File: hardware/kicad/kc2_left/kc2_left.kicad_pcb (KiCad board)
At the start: 2 copper layers, 147.2 x 133.8 mm, 70 parts, among them SW1 KEY_01, SW10 KEY_10, SW11 KEY_11, SW12 KEY_12, SW13 KEY_13, SW14 KEY_14, SW15 KEY_15, SW16 KEY_16, SW17 KEY_17, SW18 KEY_18, SW19 KEY_19, SW2 KEY_02, SW20 KEY_20, SW21 KEY_21, SW22 KEY_22, SW23 KEY_23, SW24 KEY_24, SW25 KEY_25, SW26 KEY_26, SW27 KEY_27, SW28 KEY_28, SW29 KEY_29, SW3 KEY_03, SW30 KEY_30, SW31 KEY_31, SW32 KEY_32, SW4 KEY_04, SW5 KEY_05, SW6 KEY_06, SW7 KEY_07, SW8 KEY_08, SW9 KEY_09, U1 nice!nano_v2_socket_24pin

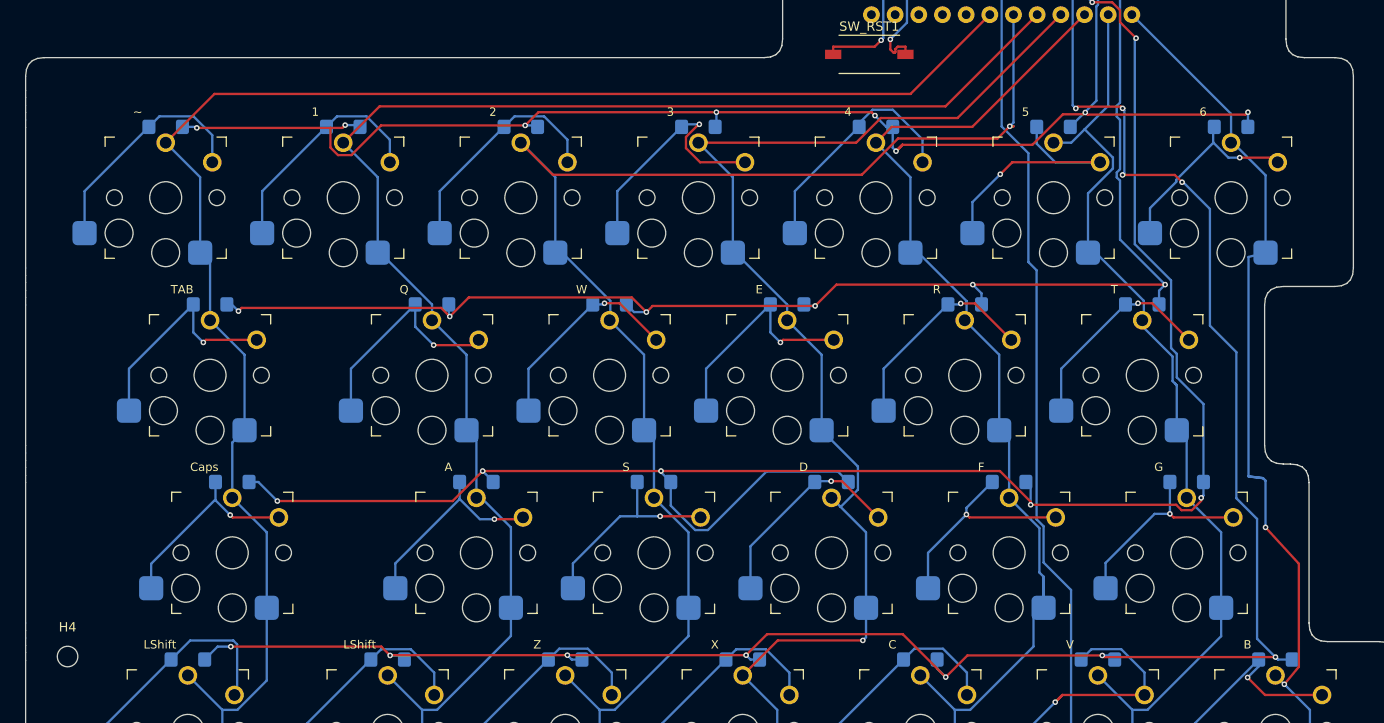
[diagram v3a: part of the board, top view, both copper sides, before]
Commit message: fix: KC2 X3 H4/H5 마운팅 홀 배치 조정
H4를 한 줄 위로 옮기고 H2 인접 상단 코너에 H5를 추가해 하부 바닥판 고정 지점 분포를 개선
왼쪽은 상단 외곽 제약 때문에 H2.x보다 안쪽인 x=173.45에 H5를 배치
관련 산출물과 검증 증거를 동일 보드 상태로 재생성
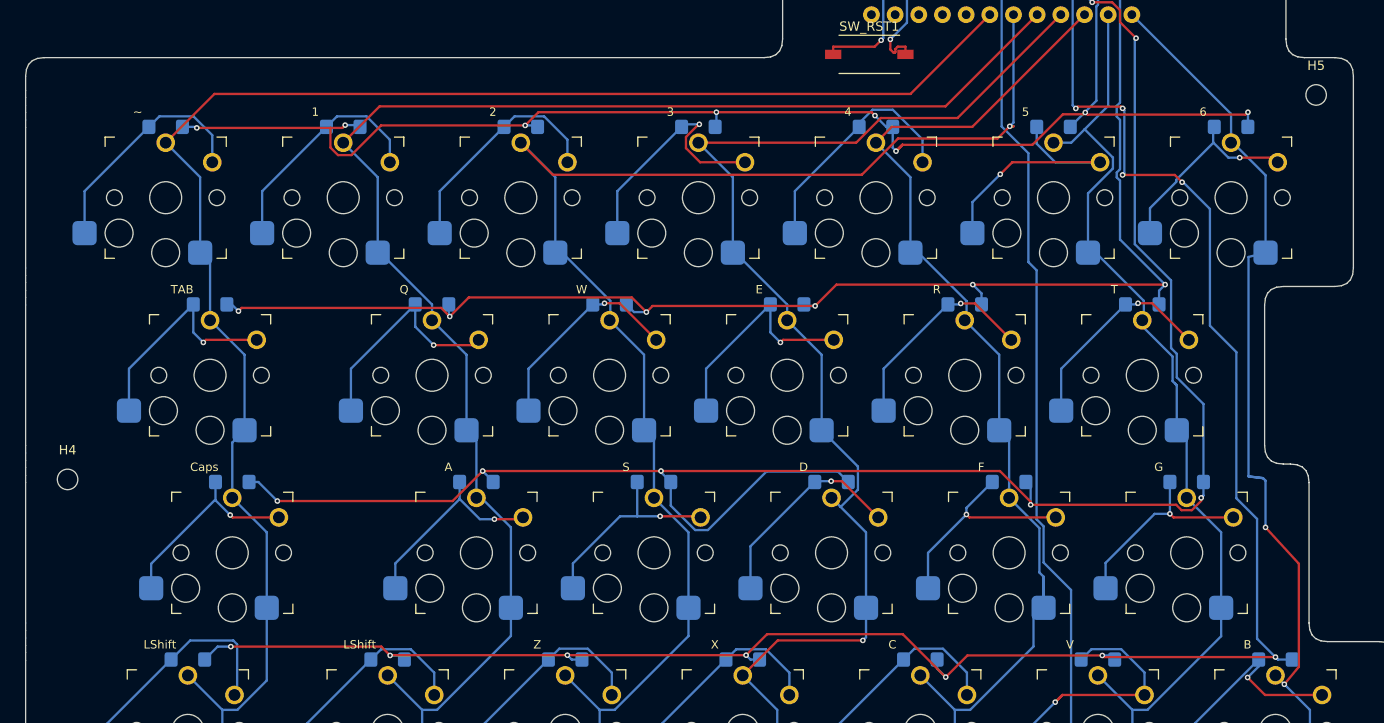
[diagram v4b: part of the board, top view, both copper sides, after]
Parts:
- added H5: M2_NPTH_2.2, MountingHole_2.2mm_M2, F.Cu at (173.4, 66.5)
- moved H4 19.0 mm to (39.5, 107.8)
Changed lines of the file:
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@@
 	(footprint "MountingHole_2.2mm_M2"
 		(layer "F.Cu")
-		(at 39.5 126.75)
+		(at 39.5 107.75)
 		(descr "Mounting Hole 2.2mm, M2, no annular, generated by kicad-footprint-generator mountinghole.py")
 		(tags "mountinghole M2")
@@
 		(embedded_fonts no)
 	)
+	(footprint "MountingHole_2.2mm_M2"
+		(layer "F.Cu")
+		(at 173.45 66.5)
+		(descr "Mounting Hole 2.2mm, M2, no annular, generated by kicad-footprint-generator mountinghole.py")
+		(tags "mountinghole M2")
+		(property "Reference" "H5"
+			(at 0 -3.15 0)
+			(layer "F.SilkS")
+			(effects
+				(font
+					(size 1 1)
+					(thickness 0.15)
+				)
+			)
+		)
+		(property "Value" "M2_NPTH_2.2"
+			(at 0 3.15 0)
+			(layer "F.Fab")
+			(effects
+				(font
+					(size 1 1)
+					(thickness 0.15)
+				)
+			)
+		)
+		(property "Datasheet" ""
+			(at 0 0 0)
+			(layer "F.Fab")
+			(hide yes)
+			(effects
+				(font
+					(size 1.27 1.27)
+				)
+			)
+		)
+		(property "Description" ""
+			(at 0 0 0)
+			(layer "F.Fab")
+			(hide yes)
+			(effects
+				(font
+					(size 1.27 1.27)
+				)
+			)
+		)
+		(property "KiLib_Generator" "mounting_hardware/mounting_hole"
+			(at 0 0 0)
+			(layer "F.SilkS")
+			(hide yes)
+			(effects
+				(font
+					(size 1 1)
+					(thickness 0.15)
+				)
+			)
+		)
+		(attr exclude_from_pos_files exclude_from_bom)
+		(duplicate_pad_numbers_are_jumpers no)
+		(fp_circle
+			(center 0 0)
+			(end 2.2 0)
+			(stroke
+				(width 0.15)
+				(type solid)
+			)
+			(fill no)
+			(layer "Cmts.User")
+		)
+		(fp_circle
+			(center 0 0)
+			(end 2.45 0)
+			(stroke
+				(width 0.05)
+				(type solid)
+			)
+			(fill no)
+			(layer "F.CrtYd")
+		)
+		(fp_text user "${REFERENCE}"
+			(at 0 0 0)
+			(layer "F.Fab")
+			(effects
+				(font
+					(size 1 1)
+					(thickness 0.15)
+				)
+			)
+		)
+		(pad "" np_thru_hole circle
+			(at 0 0)
+			(size 2.2 2.2)
+			(drill 2.2)
+			(layers "*.Cu" "*.Mask")
+		)
+		(embedded_fonts no)
+	)
 	(footprint "SW_Kailh_Choc_V1_HotSwap_THT"
 		(layer "F.Cu")
@@
 	)
 	(gr_line
-		(start 37 124.25)
-		(end 42 124.25)
+		(start 37 105.25)
+		(end 42 105.25)
 		(stroke
 			(width 0.08)
@@
 	)
 	(gr_line
-		(start 37 129.25)
-		(end 37 124.25)
+		(start 37 110.25)
+		(end 37 105.25)
 		(stroke
 			(width 0.08)
@@
 	)
 	(gr_line
-		(start 42 124.25)
-		(end 42 129.25)
+		(start 42 105.25)
+		(end 42 110.25)
 		(stroke
 			(width 0.08)
@@
 	)
 	(gr_line
-		(start 42 129.25)
-		(end 37 129.25)
+		(start 42 110.25)
+		(end 37 110.25)
 		(stroke
 			(width 0.08)
@@
 	)
 	(gr_line
+		(start 170.95 64)
+		(end 175.95 64)
+		(stroke
+			(width 0.08)
+			(type default)
+		)
+		(layer "Cmts.User")
+	)
+	(gr_line
+		(start 170.95 69)
+		(end 170.95 64)
+		(stroke
+			(width 0.08)
+			(type default)
+		)
+		(layer "Cmts.User")
+	)
+	(gr_line
 		(start 175.7125 162.25)
 		(end 180.7125 162.25)
@@
 		(stroke
 			(width 0.08)
+			(type default)
+		)
+		(layer "Cmts.User")
+	)
+	(gr_line
+		(start 175.95 64)
+		(end 175.95 69)
+		(stroke
+			(width 0.08)
+			(type default)
+		)
+		(layer "Cmts.User")
+	)
+	(gr_line
+		(start 175.95 69)
+		(end 170.95 69)
+		(stroke
+			(width 0.08)

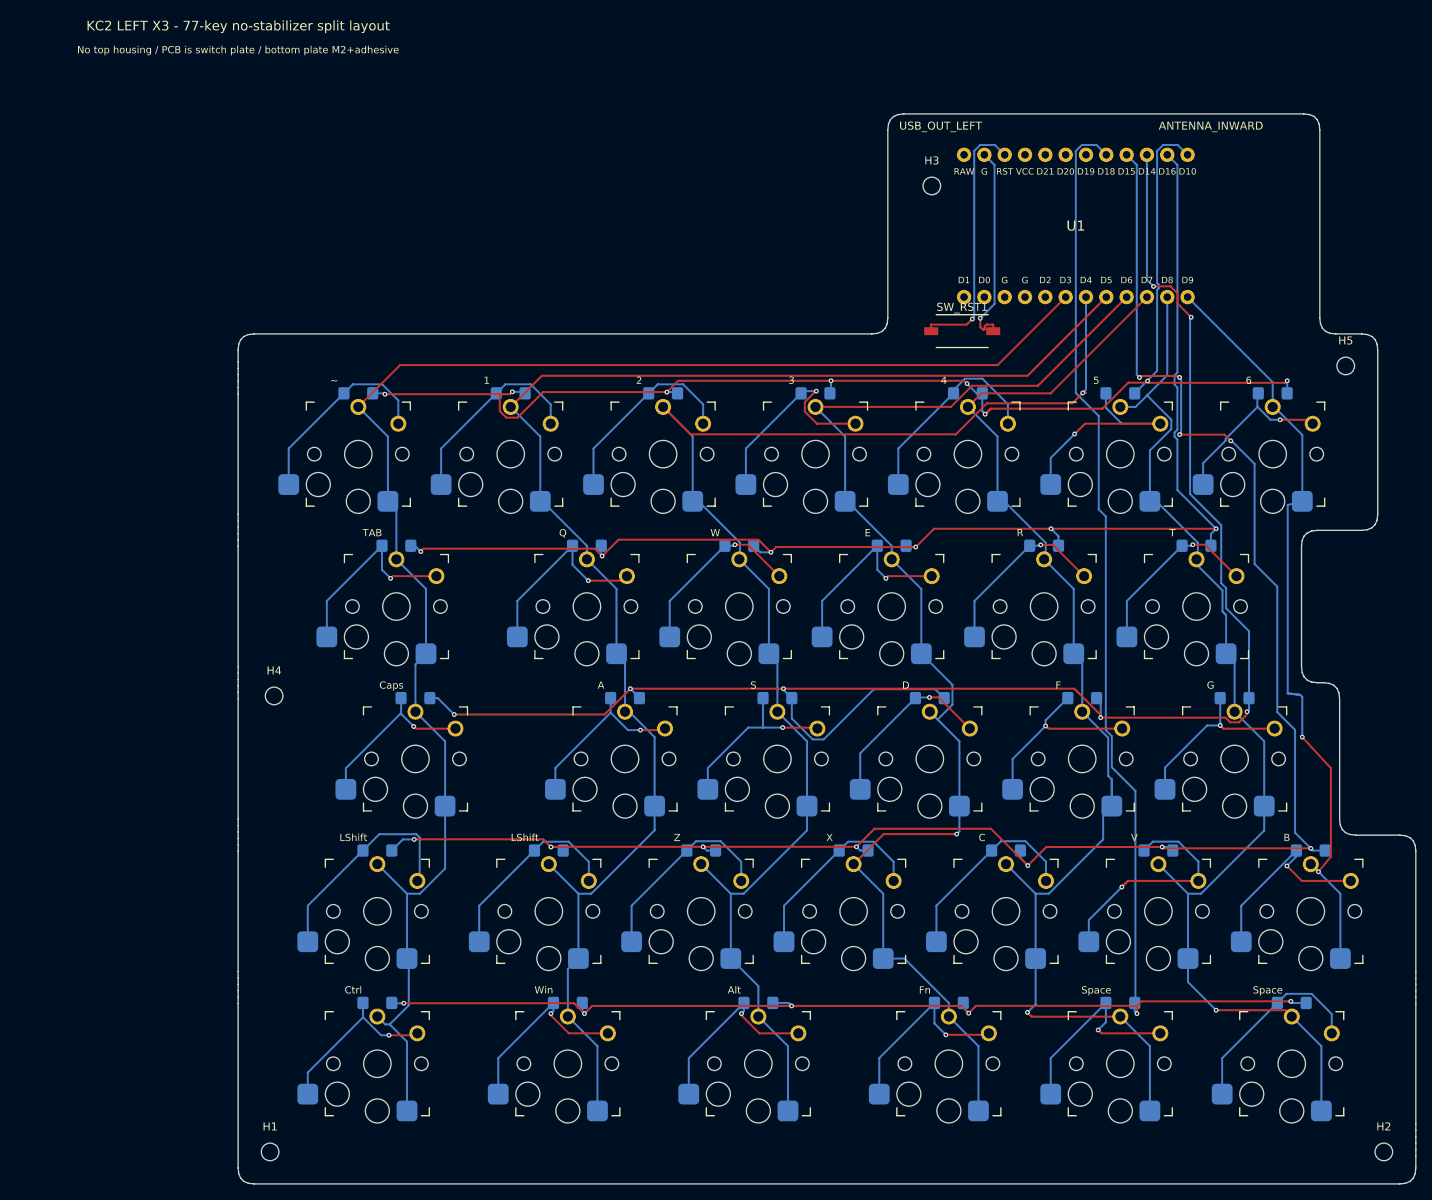
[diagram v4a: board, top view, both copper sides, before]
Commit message: feat: KC2 X3 스크류리스 주문 패키지를 주문 가능 상태로 갱신한다
스크류리스 레일 하우징용 주문 가능 상태를 확정하기 위해 M2 고정홀을 제거하고 REG_NPTH 등록홀, H1-H9 라벨, 배터리 리드 슬롯, antenna-side reset 위치, KC2 v1.0 L/R 실크를 반영한다.

DRC, 연결성, 실크 간섭, 키캡 간격, Gerber/drill/render/JLCPCB ZIP 검증기를 보강하고 주문 산출물을 재생성한다.

SpecKiwi 요구사항 증거와 Freerouting 프로세스 안전 규칙을 함께 갱신한다.
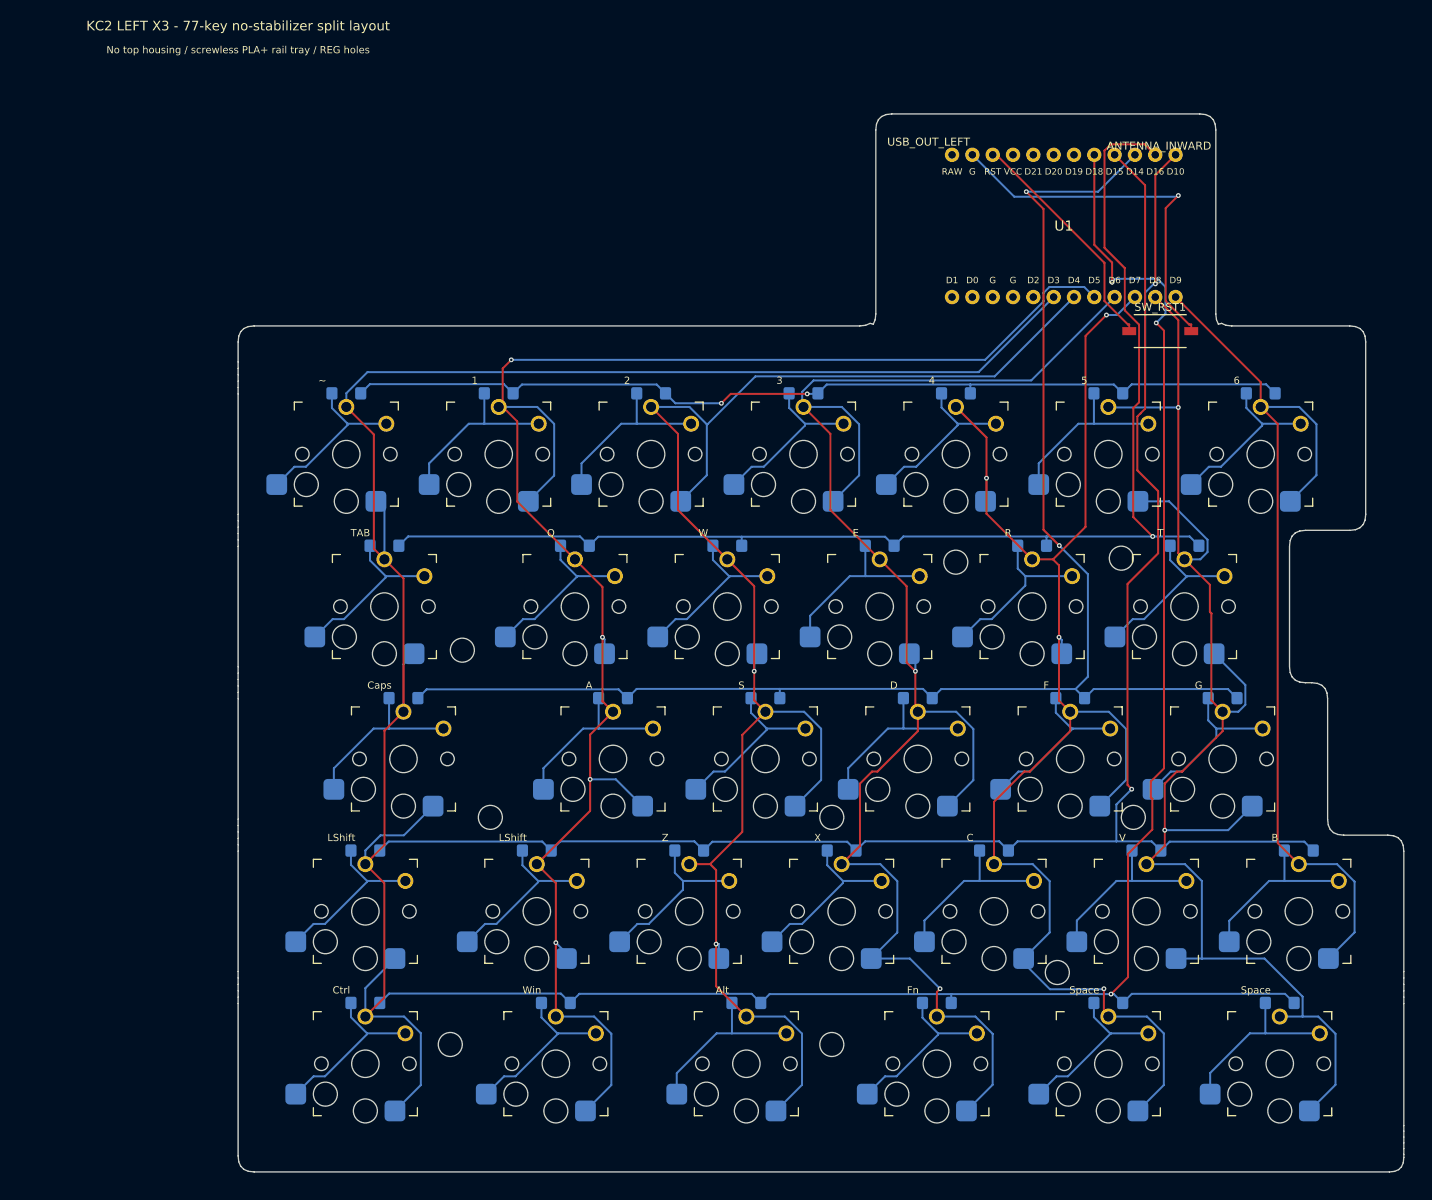
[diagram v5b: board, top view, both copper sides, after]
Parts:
- removed H1, H2, H3, H4, H5: M2_NPTH_2.2, MountingHole_2.2mm_M2
- added BAT_LEAD_SLOT1: BAT_LEAD_NPTH_SLOT_3.6x2.2, BAT_LEAD_NPTH_SLOT_3.6x2.2, F.Cu at (154.1, 49.0)
- added REG1: REG_NPTH_3.0, REG_NPTH_3.0, F.Cu at (63.0, 102.0)
- added REG2: REG_NPTH_3.0, REG_NPTH_3.0, F.Cu at (124.7, 91.0)
- added REG3: REG_NPTH_3.0, REG_NPTH_3.0, F.Cu at (145.4, 90.5)
- added REG4: REG_NPTH_3.0, REG_NPTH_3.0, F.Cu at (66.5, 122.9)
- added REG5: REG_NPTH_3.0, REG_NPTH_3.0, F.Cu at (109.2, 122.9)
- added REG6: REG_NPTH_3.0, REG_NPTH_3.0, F.Cu at (146.9, 122.9)
- added REG7: REG_NPTH_3.0, REG_NPTH_3.0, F.Cu at (61.5, 151.3)
- added REG8: REG_NPTH_3.0, REG_NPTH_3.0, F.Cu at (109.2, 151.3)
- added REG9: REG_NPTH_3.0, REG_NPTH_3.0, F.Cu at (137.4, 142.3)
- moved SW_RST1 24.7 mm to (150.3, 62.1)
- moved D1 1.50 mm to (48.5, 69.9)
- moved D10 1.50 mm to (96.2, 89.0)
- moved D11 1.50 mm to (115.2, 89.0)
- moved D12 1.50 mm to (134.2, 89.0)
- moved D13 1.50 mm to (153.3, 89.0)
- moved D15 1.50 mm to (81.9, 108.0)
- moved D16 1.50 mm to (100.9, 108.0)
- moved D17 1.50 mm to (120.0, 108.0)
- moved D18 1.50 mm to (139.0, 108.0)
- moved D19 1.50 mm to (158.1, 108.0)
- moved D2 1.50 mm to (67.6, 69.9)
- moved D20 1.50 mm to (50.9, 127.1)
- moved D21 1.50 mm to (72.3, 127.1)
- moved D22 1.50 mm to (91.4, 127.1)
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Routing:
- net L_COL5: track 138.0 -> 183.2 mm, vias 1 -> 2
- net L_COL3: track 161.9 -> 205.0 mm, vias 1 -> 2
- net L_COL0: track 199.8 -> 233.8 mm
- net L_COL1: track 188.2 -> 221.8 mm, vias 0 -> 4
- net L_COL4: track 150.9 -> 184.2 mm, vias 1 -> 4
- net L_ROW2: track 215.0 -> 188.8 mm, vias 7 -> 2
- net L_COL2: track 178.8 -> 203.0 mm, vias 1 -> 2
- net L_ROW3: track 235.7 -> 213.8 mm, vias 11 -> 1
- net GND: track 25.8 -> 47.0 mm
- net L_ROW0: track 169.8 -> 150.5 mm, vias 8 -> 3
- net L_COL6: track 97.7 -> 115.0 mm, vias 2 -> 0
- net LK25_D: track 31.3 -> 22.2 mm, vias 1 -> 0
- net LK20_D: track 27.9 -> 21.5 mm
- net LK06_D: track 28.2 -> 22.2 mm, vias 1 -> 0
- net LK04_D: track 26.4 -> 21.6 mm, vias 1 -> 0
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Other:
- board size 147.2 x 133.8 mm -> 145.7 x 132.2 mm
- board text added: "BAT LEAD EXIT"
- board text added: "H1"
- board text added: "H2"
- board text added: "H3"
- board text added: "H4"
- board text added: "H5"
- board text added: "H6"
- board text added: "H7"
- board text added: "H8"
- board text added: "H9"
- board text added: "KC2 v1.0 L"
- board text added: "No top housing / screwless PLA+ rail tray / REG holes"
- board text removed: "No top housing / PCB is switch plate / bottom plate M2+adhesive"
